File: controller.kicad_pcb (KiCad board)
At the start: 4 copper layers, 46 x 53 mm, 134 parts, among them IC1 TJA1050T_CM,118, IC2 STSPIN32G4, IC3 AS5600-ASOM, IC4 AS5600-ASOM, J1 XT30XT30PW_MALE, J2 XT30XT30PW_MALE, M1 MOUNT, M2 MOUNT, M3 MOUNT, M4 MOUNT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

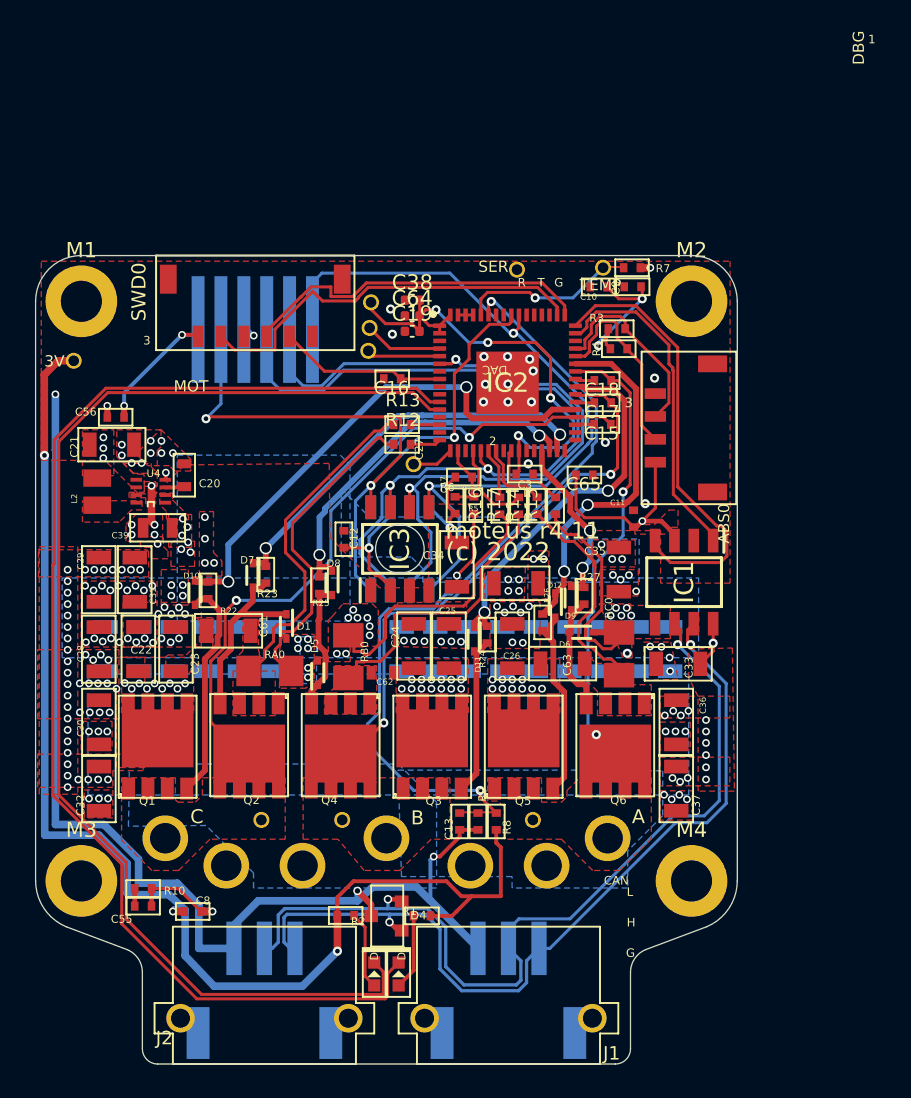
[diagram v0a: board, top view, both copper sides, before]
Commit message: Slightly cheaper
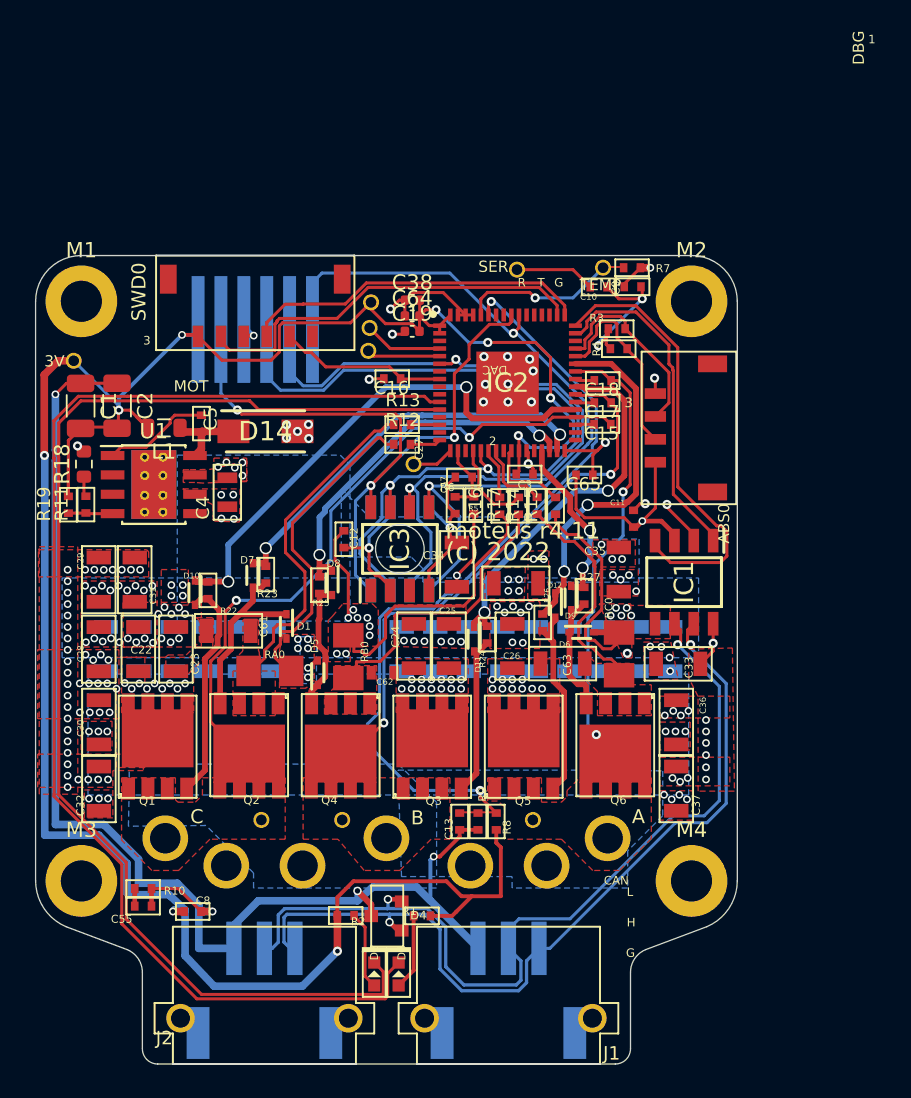
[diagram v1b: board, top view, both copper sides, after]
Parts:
- removed C20: 1uF, controller:C0603
- removed C21: 10uF, controller:C1206
- removed C39: 1uF 100V, controller:C0805
- removed C56: 1uF, controller:C0402
- removed L2: LBM2016T120J, inductor:INDC2016X180N
- removed U4: MAX15062AATA+T, controller:21-0487A_MXM
- added C1: 100uF, Capacitor_SMD:C_1206_3216Metric, F.Cu at (128.4, 88.4)
- added C2: 100uF, Capacitor_SMD:C_1206_3216Metric, F.Cu at (130.8, 88.3)
- added C4: 10uF, controller:C0805, F.Cu at (138.1, 94.0)
- added C5: 0.01uF, controller:C0402, F.Cu at (136.4, 89.5)
- added D14: SS14, SamacSys:DIOM5127X261N, F.Cu at (140.6, 90.0)
- added L1: 22uH, Inductor_SMD:L_0805_2012Metric, F.Cu at (133.9, 89.8)
- added R11: 5.6k, controller:R0402, F.Cu at (128.8, 94.8)
- added R18: 270, Resistor_SMD:R_0603_1608Metric, F.Cu at (128.7, 92.2)
- added R19: 10k, controller:R0402, F.Cu at (127.7, 94.8)
- added U1: TPS5430DDAR, Package_SO:TI_SO-PowerPAD-8_ThermalVias, F.Cu at (133.2, 93.5)
- R1, R2: value 560 -> 510
- R22, R23, R24, R25, R26, R27: value 7.5 -> 10
- R5: value 100k 1% -> 100k
- R6: value 4.7k 1% -> 4.7k
- R7, R9: value 10k 1% -> 10k
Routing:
- net GND: track 105.9 -> 145.3 mm, vias 126 -> 118
- net +3V3: track 159.4 -> 192.3 mm, vias 17 -> 13
- net Net-(U1-BOOT): track 0.00 -> 7.05 mm
- net Net-(U1-PH): track 0.00 -> 5.35 mm
- net Net-(U1-VSENSE): track 0.00 -> 2.92 mm
- net /AS5047_DIR: track 50.5 -> 48.1 mm
- net Net-(R11-PadP$2): track 0.00 -> 1.36 mm
- net Net-(U4-VCC): track 1.27 -> 0.00 mm
- net /SWDIO: track 23.4 -> 22.8 mm
- net V+: vias 106 -> 105
- removed copper zone on F.Cu, net +3V3
- removed copper zone on F.Cu, net /VSW

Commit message: Almost?
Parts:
- removed C1, C2: 100uF, Capacitor_SMD:C_1206_3216Metric
- removed C4: 10uF, controller:C0805
- removed C5: 0.01uF, controller:C0402
- removed C64: 100nF, Capacitor_SMD:C_0402_1005Metric
- removed C65: 100nF, controller:C0402
- removed L1: 22uH, Inductor_SMD:L_0805_2012Metric
- removed R11: 5.6k, controller:R0402
- removed R15: 1k, controller:R0402
- removed R18: 270, Resistor_SMD:R_0603_1608Metric
- removed R19: 10k, controller:R0402
- removed TEMP1: PAD24AWG_PAD, controller:24AWG_PAD
- removed U1: TPS5430DDAR, Package_SO:TI_SO-PowerPAD-8_ThermalVias
- added C14: 10uF, Capacitor_SMD:C_0402_1005Metric, F.Cu at (156.0, 80.0)
- added C20: 100nF, Capacitor_SMD:C_0402_1005Metric, F.Cu at (149.5, 81.0)
- added C21: 100nF, controller:C0402, F.Cu at (158.4, 94.7)
- added C39: 100nF, controller:C0402, F.Cu at (153.9, 80.0)
- added C6: 200nF / 100V, Capacitor_SMD:C_1210_3225Metric, F.Cu at (148.1, 84.8)
- added C7: 10uF, Capacitor_SMD:C_0402_1005Metric, F.Cu at (146.2, 87.9)
- added L2: 18uH/1A, EasyEda2Kicad:IND-SMD_L5.8-W5.2_SCD0503T, F.Cu at (141.7, 89.4)
- added R20: 1.5k, controller:R0402, F.Cu at (156.2, 97.7)
- added R21: 1.5k, controller:R0402, F.Cu at (155.0, 97.7)
- added R28: 22k, controller:R0402, F.Cu at (155.6, 96.0)
- added R29: 22k, controller:R0402, F.Cu at (158.4, 95.9)
- added R30: 11k, controller:R0402, F.Cu at (155.5, 93.5)
- added R31: 1.5k, controller:R0402, F.Cu at (160.8, 97.8)
- added R32: 1.5k, controller:R0402, F.Cu at (160.8, 96.5)
- added R33: 22k, controller:R0402, F.Cu at (155.6, 94.8)
- added R34: 22k, controller:R0402, F.Cu at (158.4, 97.1)
- added R35: 11k, controller:R0402, F.Cu at (160.4, 93.5)
- C38: value 10uF -> 1uF; footprint Capacitor_SMD:C_0402_1005Metric -> controller:C0402
- D14: value SS14 -> D_Schottky; footprint SamacSys:DIOM5127X261N -> Diode_SMD:D_SMA
- R12, R13: value 1k -> 22k
- R14, R16: value 1k -> 1.5k
- R17: value 1k -> 11k
- moved DG2 30.0 mm to (128.0, 86.9)
- moved R14 16.0 mm to (143.0, 99.4), turned to -90 degrees
- moved R16 14.8 mm to (141.8, 99.5), turned to -90 degrees
- moved R17 8.75 mm to (149.8, 90.1), turned to 0 degrees
- moved DAC0 8.73 mm to (143.0, 97.0)
- moved D14 6.96 mm to (135.1, 94.3), turned to -90 degrees
- moved DBG1 6.00 mm to (145.9, 89.1)
- moved DBG2 5.85 mm to (145.9, 90.4)
- moved C19 3.49 mm to (149.5, 80.0), turned to 180 degrees
- moved R13 2.34 mm to (147.5, 90.8), turned to 90 degrees
- moved C38 1.99 mm to (151.6, 80.0)
- moved C16 1.82 mm to (150.7, 86.2), turned to -90 degrees
- moved TEMP2 1.54 mm to (161.2, 79.3)
- moved C3 1.05 mm to (158.6, 93.1)
- moved R12 0.52 mm to (149.3, 91.4), turned to 180 degrees
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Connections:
- D14 pad 1: Net-(U1-PH) -> Net-(D14-K)
- IC2 pad 14: Net-(IC2-PA1) -> /PA1
- IC2 pad 15: unconnected-(IC2-PA2-Pad15) -> /PA2
- IC2 pad 16: Net-(IC2-PA3) -> /PA3
- IC2 pad 19: unconnected-(IC2-PA6-Pad19) -> /PA6
- IC2 pad 20: Net-(IC2-PA7) -> /PA7
- IC2 pad 22: Net-(IC2-PC5) -> /PC5
- IC2 pad 23: Net-(IC2-PB0) -> /PB0
- IC2 pad 24: unconnected-(IC2-PB1-Pad24) -> /PB1
- IC2 pad 25: Net-(IC2-PB2) -> /PB2
- IC2 pad 27: GND -> +3V3
- IC2 pad 61: GND -> V+
- IC2 pad 62: GND -> Net-(D14-K)
- IC2 pad 63: GND -> Net-(IC2-REGIN)
- IC2 pad 64: +3V3 -> Net-(IC2-REGIN)
- R12 pad P$1: /SXA_N -> V+
- R12 pad P$2: Net-(IC2-PA3) -> /PA1
- R13 pad P$1: /SXA_P -> /PA1
- R13 pad P$2: Net-(IC2-PA1) -> GND
- R14 pad P$1: /SXC_P -> /PA3
- R14 pad P$2: Net-(IC2-PB0) -> /SXA_N
- R16 pad P$1: /SXB_N -> /PA1
- R16 pad P$2: Net-(IC2-PC5) -> /SXA_P
- R17 pad P$1: /SXB_P -> GND
- R17 pad P$2: Net-(IC2-PA7) -> /PA2
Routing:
- net V+: track 5.16 -> 52.4 mm, vias 105 -> 99
- net GND: track 145.3 -> 186.3 mm, vias 118 -> 108
- net /PA1: track 0.00 -> 26.2 mm, vias 0 -> 2
- net Net-(D14-K): track 0.00 -> 25.5 mm
- net Net-(IC2-REGIN): track 0.00 -> 16.7 mm
- net +3V3: track 192.3 -> 176.2 mm
- net /SXA_P: track 20.3 -> 6.40 mm
- net /SXA_N: track 19.5 -> 6.01 mm
- net /PA3: track 0.00 -> 13.3 mm, vias 0 -> 2
- net /PB0: track 0.00 -> 13.0 mm
- net /DAC: track 2.77 -> 14.9 mm, vias 0 -> 2
- net /PA7: track 0.00 -> 9.38 mm, vias 0 -> 2
- net /PB2: track 0.00 -> 8.88 mm, vias 0 -> 2
- net Net-(U1-BOOT): track 7.05 -> 0.00 mm
- net /DEBUG2: track 4.82 -> 11.3 mm, vias 0 -> 1
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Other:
- board text added: "GND"
- board text removed: "(c) 2022"
- board text removed: "SER"
- board text removed: "moteus r4.11"
